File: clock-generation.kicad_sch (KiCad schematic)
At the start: 28 parts, among them U1 Si5351B-B-GM, U2 TPS79301-EP, U3 DAC53002RTER, Y1 7M-27.000MEEQ-T

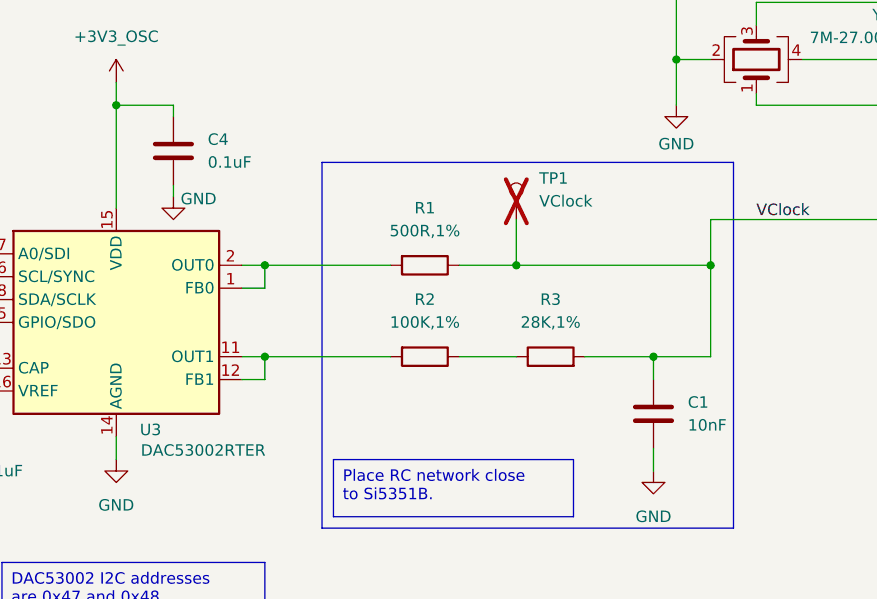
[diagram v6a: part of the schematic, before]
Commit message: worked through ERCs and updated PCB components
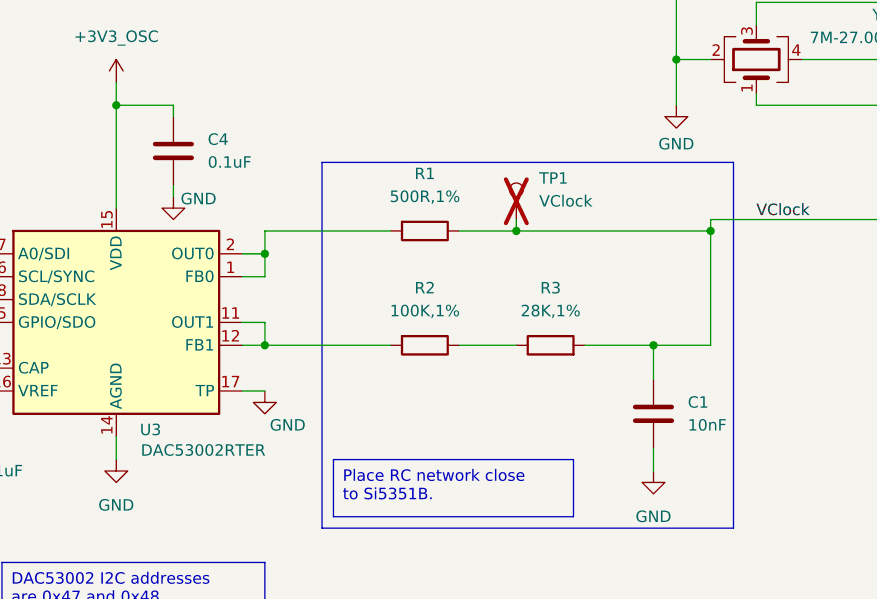
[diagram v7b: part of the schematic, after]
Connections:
- net GND: now also U3.17 (TP)
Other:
- moved on the sheet: R1, R2, R3
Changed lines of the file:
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@@
 	)
 	(junction
-		(at 95.25 55.88)
+		(at 143.51 114.3)
 		(diameter 0)
 		(color 0 0 0 0)
 	)
 	(junction
-		(at 143.51 118.11)
+		(at 95.25 55.88)
 		(diameter 0)
 		(color 0 0 0 0)
@@
 	)
 	(junction
-		(at 93.98 118.11)
-		(diameter 0)
-		(color 0 0 0 0)
-	)
-	(junction
-		(at 121.92 118.11)
+		(at 93.98 116.84)
 		(diameter 0)
 		(color 0 0 0 0)
@@
 	)
 	(junction
-		(at 93.98 128.27)
+		(at 227.33 92.71)
 		(diameter 0)
 		(color 0 0 0 0)
 	)
 	(junction
-		(at 227.33 92.71)
+		(at 137.16 127)
 		(diameter 0)
 		(color 0 0 0 0)
@@
 	)
 	(junction
+		(at 93.98 127)
+		(diameter 0)
+		(color 0 0 0 0)
+	)
+	(junction
 		(at 194.31 85.09)
 		(diameter 0)
@@
 	)
 	(junction
-		(at 137.16 128.27)
+		(at 95.25 45.72)
 		(diameter 0)
 		(color 0 0 0 0)
 	)
 	(junction
-		(at 95.25 45.72)
+		(at 109.22 45.72)
 		(diameter 0)
 		(color 0 0 0 0)
 	)
 	(junction
-		(at 109.22 45.72)
+		(at 121.92 114.3)
 		(diameter 0)
 		(color 0 0 0 0)
@@
 	(wire
 		(pts
-			(xy 137.16 128.27) (xy 129.54 128.27)
+			(xy 137.16 127) (xy 129.54 127)
 		)
 		(stroke
@@
 	(wire
 		(pts
-			(xy 93.98 128.27) (xy 107.95 128.27)
+			(xy 93.98 127) (xy 107.95 127)
 		)
 		(stroke
@@
 	(wire
 		(pts
-			(xy 121.92 118.11) (xy 115.57 118.11)
+			(xy 121.92 114.3) (xy 115.57 114.3)
 		)
 		(stroke
@@
 	(wire
 		(pts
-			(xy 143.51 113.03) (xy 143.51 118.11)
+			(xy 143.51 113.03) (xy 143.51 114.3)
 		)
 		(stroke
@@
 	(wire
 		(pts
-			(xy 115.57 128.27) (xy 121.92 128.27)
+			(xy 115.57 127) (xy 121.92 127)
+		)
+		(stroke
+			(width 0)
+			(type default)
+		)
+	)
+	(wire
+		(pts
+			(xy 93.98 114.3) (xy 93.98 116.84)
 		)
 		(stroke
@@
 	(wire
 		(pts
-			(xy 143.51 118.11) (xy 121.92 118.11)
+			(xy 143.51 114.3) (xy 121.92 114.3)
 		)
 		(stroke
@@
 	(wire
 		(pts
-			(xy 93.98 118.11) (xy 93.98 120.65)
+			(xy 93.98 116.84) (xy 93.98 119.38)
 		)
 		(stroke
@@
 	(wire
 		(pts
-			(xy 93.98 130.81) (xy 91.44 130.81)
+			(xy 93.98 127) (xy 91.44 127)
 		)
 		(stroke
@@
 	(wire
 		(pts
+			(xy 143.51 114.3) (xy 143.51 127)
+		)
+		(stroke
+			(width 0)
+			(type default)
+		)
+	)
+	(wire
+		(pts
 			(xy 83.82 101.6) (xy 83.82 100.33)
 		)
@@
 	(wire
 		(pts
-			(xy 93.98 120.65) (xy 91.44 120.65)
+			(xy 93.98 119.38) (xy 91.44 119.38)
 		)
 		(stroke
@@
 	(wire
 		(pts
-			(xy 91.44 128.27) (xy 93.98 128.27)
+			(xy 91.44 124.46) (xy 93.98 124.46)
 		)
 		(stroke
@@
 	(wire
 		(pts
-			(xy 93.98 128.27) (xy 93.98 130.81)
+			(xy 93.98 124.46) (xy 93.98 127)
 		)
 		(stroke
@@
 	(wire
 		(pts
-			(xy 93.98 118.11) (xy 107.95 118.11)
+			(xy 93.98 114.3) (xy 107.95 114.3)
 		)
 		(stroke
@@
 	(wire
 		(pts
+			(xy 137.16 127) (xy 137.16 130.81)
+		)
+		(stroke
+			(width 0)
+			(type default)
+		)
+	)
+	(wire
+		(pts
 			(xy 191.77 68.58) (xy 198.12 68.58)
 		)
@@
 	(wire
 		(pts
-			(xy 137.16 128.27) (xy 137.16 130.81)
-		)
-		(stroke
-			(width 0)
-			(type default)
-		)
-	)
-	(wire
-		(pts
 			(xy 80.01 66.04) (xy 80.01 68.58)
 		)
@@
 	(wire
 		(pts
-			(xy 91.44 118.11) (xy 93.98 118.11)
+			(xy 91.44 116.84) (xy 93.98 116.84)
 		)
 		(stroke
@@
 	(wire
 		(pts
-			(xy 229.87 68.58) (xy 242.57 68.58)
+			(xy 93.98 132.08) (xy 91.44 132.08)
 		)
 		(stroke
@@
 	(wire
 		(pts
-			(xy 143.51 118.11) (xy 143.51 128.27)
+			(xy 229.87 68.58) (xy 242.57 68.58)
 		)
 		(stroke
@@
 	(wire
 		(pts
-			(xy 121.92 113.03) (xy 121.92 118.11)
+			(xy 121.92 113.03) (xy 121.92 114.3)
 		)
 		(stroke
@@
 	(wire
 		(pts
-			(xy 143.51 128.27) (xy 137.16 128.27)
+			(xy 143.51 127) (xy 137.16 127)
 		)
 		(stroke
@@
 	)
 	(symbol
+		(lib_id "power:GND")
+		(at 93.98 132.08 0)
+		(unit 1)
+		(exclude_from_sim no)
+		(in_bom yes)
+		(on_board yes)
+		(dnp no)
+		(property "Reference" "#PWR061"
+			(at 93.98 138.43 0)
+			(effects
+				(font
+					(size 1.27 1.27)
+				)
+				(hide yes)
+			)
+		)
+		(property "Value" "GND"
+			(at 96.52 135.89 0)
+			(effects
+				(font
+					(size 1.27 1.27)
+				)
+			)
+		)
+		(property "Footprint" ""
+			(at 93.98 132.08 0)
+			(effects
+				(font
+					(size 1.27 1.27)
+				)
+				(hide yes)
+			)
+		)
+		(property "Datasheet" ""
+			(at 93.98 132.08 0)
+			(effects
+				(font
+					(size 1.27 1.27)
+				)
+				(hide yes)
+			)
+		)
+		(property "Description" "Power symbol creates a global label with name \"GND\" , ground"
+			(at 93.98 132.08 0)
+			(effects
+				(font
+					(size 1.27 1.27)
+				)
+				(hide yes)
+			)
+		)
+		(pin "1"
+		)
+		(instances
+			(project "jkembedded-audio-board"
+				(path "/df100556-b288-4cb1-b69f-c0734132cb90/be7c4f40-c0c2-47f2-9c0c-8904af6555df"
+					(reference "#PWR061")
+					(unit 1)
+				)
+			)
+		)
+	)
+	(symbol
 		(lib_id "Device:C")
 		(at 137.16 134.62 0)
@@
 		(pin "14"
 		)
+		(pin "17"
+		)
 		(instances
 			(project ""
@@
 	(symbol
 		(lib_id "Device:R")
-		(at 125.73 128.27 90)
+		(at 125.73 127 90)
 		(unit 1)
 		(exclude_from_sim no)
@@
 		(fields_autoplaced yes)
 		(property "Reference" "R3"
-			(at 125.73 121.92 90)
+			(at 125.73 120.65 90)
 			(effects
 				(font
@@
 		)
 		(property "Value" "28K,1%"
-			(at 125.73 124.46 90)
+			(at 125.73 123.19 90)
 			(effects
 				(font
@@
 		)
 		(property "Footprint" "Resistor_SMD:R_0603_1608Metric"
-			(at 125.73 130.048 90)
+			(at 125.73 128.778 90)
 			(effects
 				(font
@@
 		)
 		(property "Datasheet" "~"
-			(at 125.73 128.27 0)
+			(at 125.73 127 0)
 			(effects
 				(font
@@
 		)
 		(property "Description" "Resistor"
-			(at 125.73 128.27 0)
+			(at 125.73 127 0)
 			(effects
 				(font
@@
 	(symbol
 		(lib_id "Device:R")
-		(at 111.76 128.27 270)
+		(at 111.76 127 270)
 		(unit 1)
 		(exclude_from_sim no)
@@
 		(fields_autoplaced yes)
 		(property "Reference" "R2"
-			(at 111.76 121.92 90)
+			(at 111.76 120.65 90)
 			(effects
 				(font
@@
 		)
 		(property "Value" "100K,1%"
-			(at 111.76 124.46 90)
+			(at 111.76 123.19 90)
 			(effects
 				(font
@@
 		)
 		(property "Footprint" "Resistor_SMD:R_0603_1608Metric"
-			(at 111.76 126.492 90)
+			(at 111.76 125.222 90)
 			(effects
 				(font
@@
 		)
 		(property "Datasheet" "~"
-			(at 111.76 128.27 0)
+			(at 111.76 127 0)
 			(effects
 				(font
@@
 		)
 		(property "Description" "Resistor"
-			(at 111.76 128.27 0)
+			(at 111.76 127 0)
 			(effects
 				(font
@@
 	(symbol
 		(lib_id "Device:R")
-		(at 111.76 118.11 270)
+		(at 111.76 114.3 270)
 		(unit 1)
 		(exclude_from_sim no)
@@
 		(on_board yes)
 		(dnp no)
-		(fields_autoplaced yes)
 		(property "Reference" "R1"
-			(at 111.76 111.76 90)
+			(at 111.76 107.95 90)
 			(effects
 				(font
@@
 		)
 		(property "Value" "500R,1%"
-			(at 111.76 114.3 90)
+			(at 111.76 110.49 90)
 			(effects
 				(font
@@
 		)
 		(property "Footprint" "Resistor_SMD:R_0603_1608Metric"
-			(at 111.76 116.332 90)
+			(at 111.76 112.522 90)
 			(effects
 				(font
@@
 		)
 		(property "Datasheet" "~"
-			(at 111.76 118.11 0)
+			(at 111.76 114.3 0)
 			(effects
 				(font
@@
 		)
 		(property "Description" "Resistor"
-			(at 111.76 118.11 0)
+			(at 111.76 114.3 0)
 			(effects
 				(font

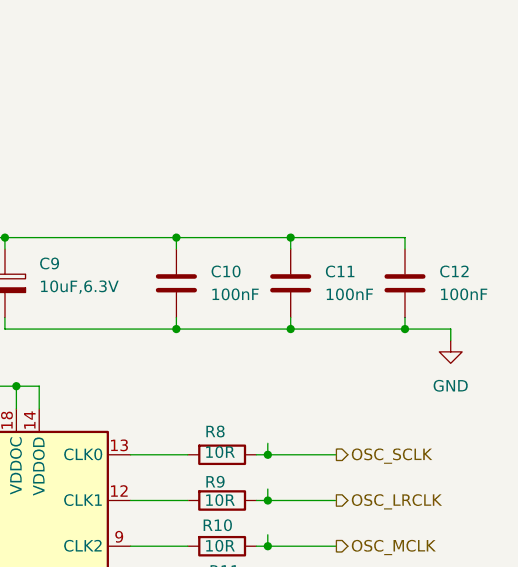
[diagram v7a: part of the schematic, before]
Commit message: Resolved #7: swapped click board header connections and finished first pass routing
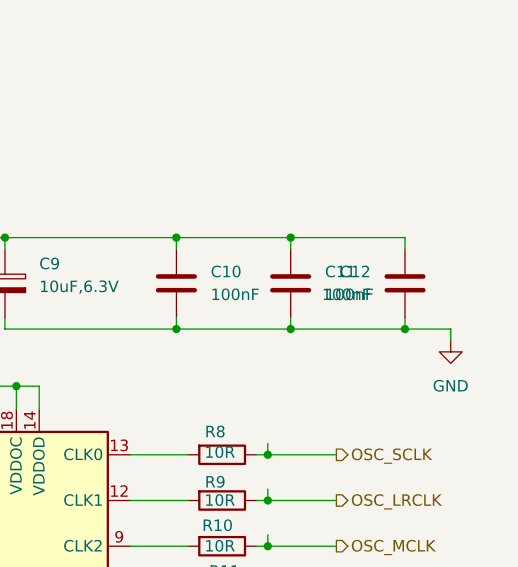
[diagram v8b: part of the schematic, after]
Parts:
- R10, R11, R8, R9: footprint Resistor_SMD:R_0402_1005Metric -> Resistor_SMD:R_0603_1608Metric
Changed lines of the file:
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@@
 		(lib_id "Device:C")
 		(at 242.57 73.66 0)
-		(unit 1)
-		(exclude_from_sim no)
-		(in_bom yes)
-		(on_board yes)
-		(dnp no)
-		(fields_autoplaced yes)
+		(mirror y)
+		(unit 1)
+		(exclude_from_sim no)
+		(in_bom yes)
+		(on_board yes)
+		(dnp no)
 		(property "Reference" "C12"
-			(at 246.38 72.3899 0)
+			(at 238.76 72.3899 0)
 			(effects
 				(font
@@
 		)
 		(property "Value" "100nF"
-			(at 246.38 74.9299 0)
+			(at 238.76 74.9299 0)
 			(effects
 				(font
@@
 		)
 		(property "Footprint" "Capacitor_SMD:C_0603_1608Metric"
-			(at 243.5352 77.47 0)
+			(at 241.6048 77.47 0)
 			(effects
 				(font
@@
 			)
 		)
-		(property "Footprint" "Resistor_SMD:R_0402_1005Metric"
+		(property "Footprint" "Resistor_SMD:R_0603_1608Metric"
 			(at 222.25 106.172 90)
 			(effects
@@
 			)
 		)
-		(property "Footprint" "Resistor_SMD:R_0402_1005Metric"
+		(property "Footprint" "Resistor_SMD:R_0603_1608Metric"
 			(at 222.25 96.012 90)
 			(effects
@@
 			)
 		)
-		(property "Footprint" "Resistor_SMD:R_0402_1005Metric"
+		(property "Footprint" "Resistor_SMD:R_0603_1608Metric"
 			(at 222.25 101.092 90)
 			(effects
@@
 			)
 		)
-		(property "Footprint" "Resistor_SMD:R_0402_1005Metric"
+		(property "Footprint" "Resistor_SMD:R_0603_1608Metric"
 			(at 222.25 90.932 90)
 			(effects
